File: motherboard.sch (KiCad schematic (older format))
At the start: 0 parts

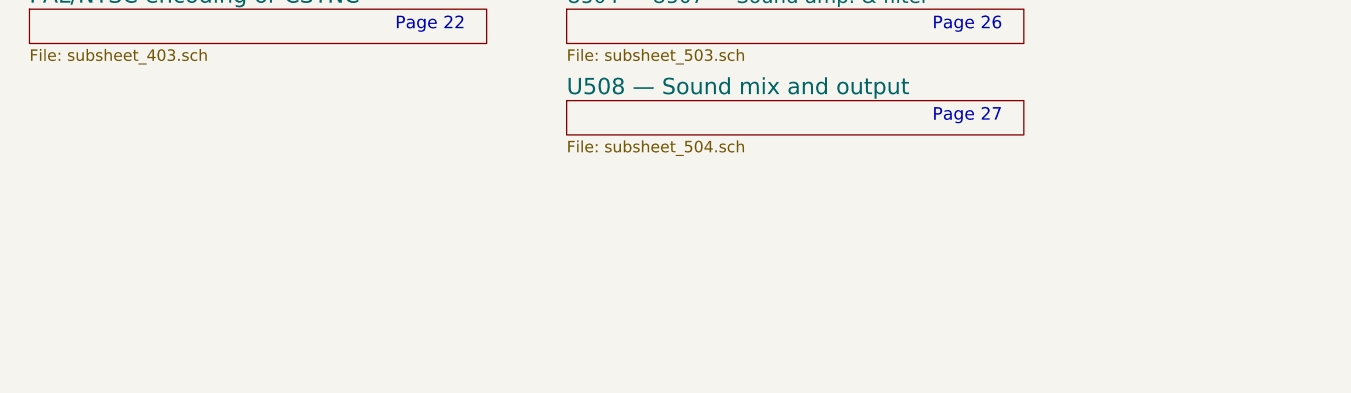
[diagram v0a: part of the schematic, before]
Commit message: Added a note about the presence of comment referencing some hardware fixes
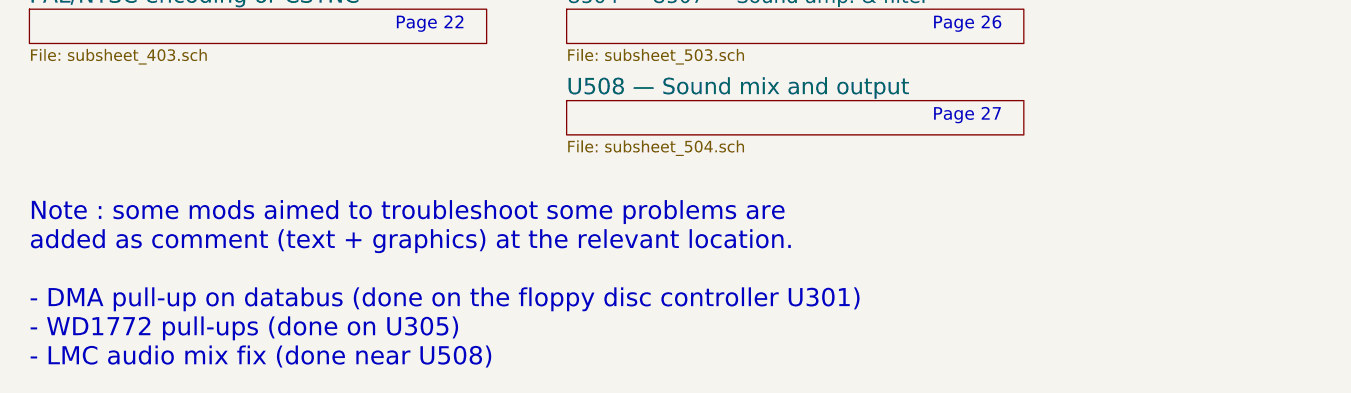
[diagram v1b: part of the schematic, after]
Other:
- note added: "Note : some mods aimed to troubleshoot some problems are \nadded as comment (text + graphics) at the relevant location.\n\n- DMA pull-up on databus (done on the floppy disc controller U301)\n- WD1772 pull-ups (done on U305)\n- LMC audio mix fix (done near U508)\n\n"
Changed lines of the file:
@@
 Text Notes 900  1500 0    500  ~ 100
 Table of content
+Text Notes 800  8800 0    79   ~ 0
+Note : some mods aimed to troubleshoot some problems are \nadded as comment (text + graphics) at the relevant location.\n\n- DMA pull-up on databus (done on the floppy disc controller U301)\n- WD1772 pull-ups (done on U305)\n- LMC audio mix fix (done near U508)\n\n
 $EndSCHEMATC
